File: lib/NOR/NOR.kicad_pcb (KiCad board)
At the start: 2 copper layers, 4 parts

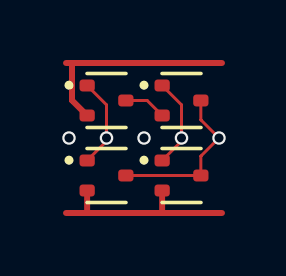
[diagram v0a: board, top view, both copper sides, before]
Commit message: High-density layout with pitch of 1.1mm, which gains 23% !!
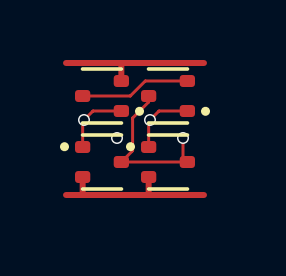
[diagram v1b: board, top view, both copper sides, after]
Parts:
- moved N2 0.64 mm to (3.30, 3.30)
- moved N1 0.47 mm to (1.10, 3.30)
- moved P2 0.47 mm to (3.30, 1.10), turned to 180 degrees
- moved P1 0.21 mm to (1.10, 1.10), turned to 180 degrees
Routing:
- net C: track 1.42 -> 3.70 mm
- net VDD: track 7.16 -> 5.19 mm
- net GND: track 6.70 -> 5.80 mm
- net B: track 3.03 -> 2.29 mm
- net A: track 3.03 -> 2.29 mm
- net (no net): vias 2 -> 1
